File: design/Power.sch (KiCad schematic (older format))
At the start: 14 parts, among them U2 TC2117

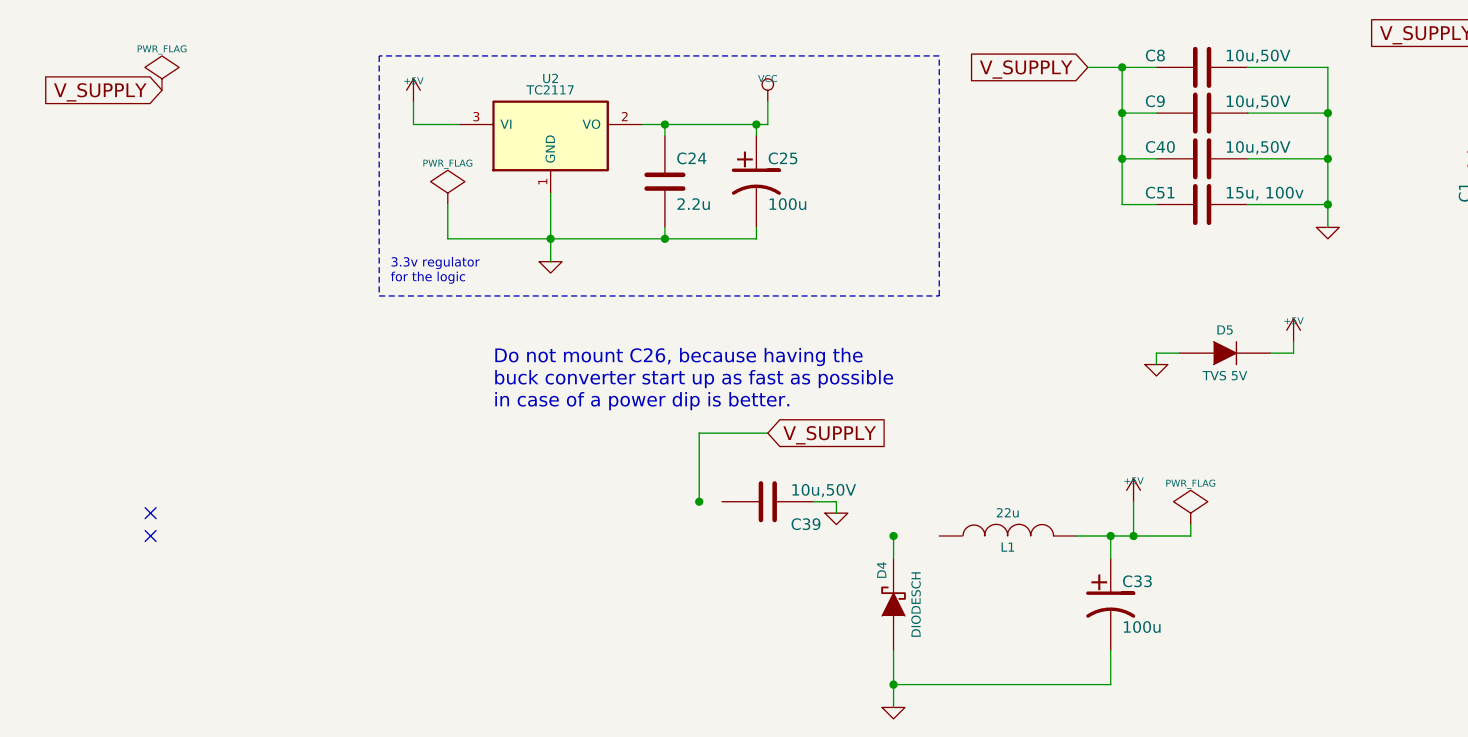
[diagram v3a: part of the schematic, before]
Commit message: Removed 5V power level. Integrated isolated CAN bus driver.
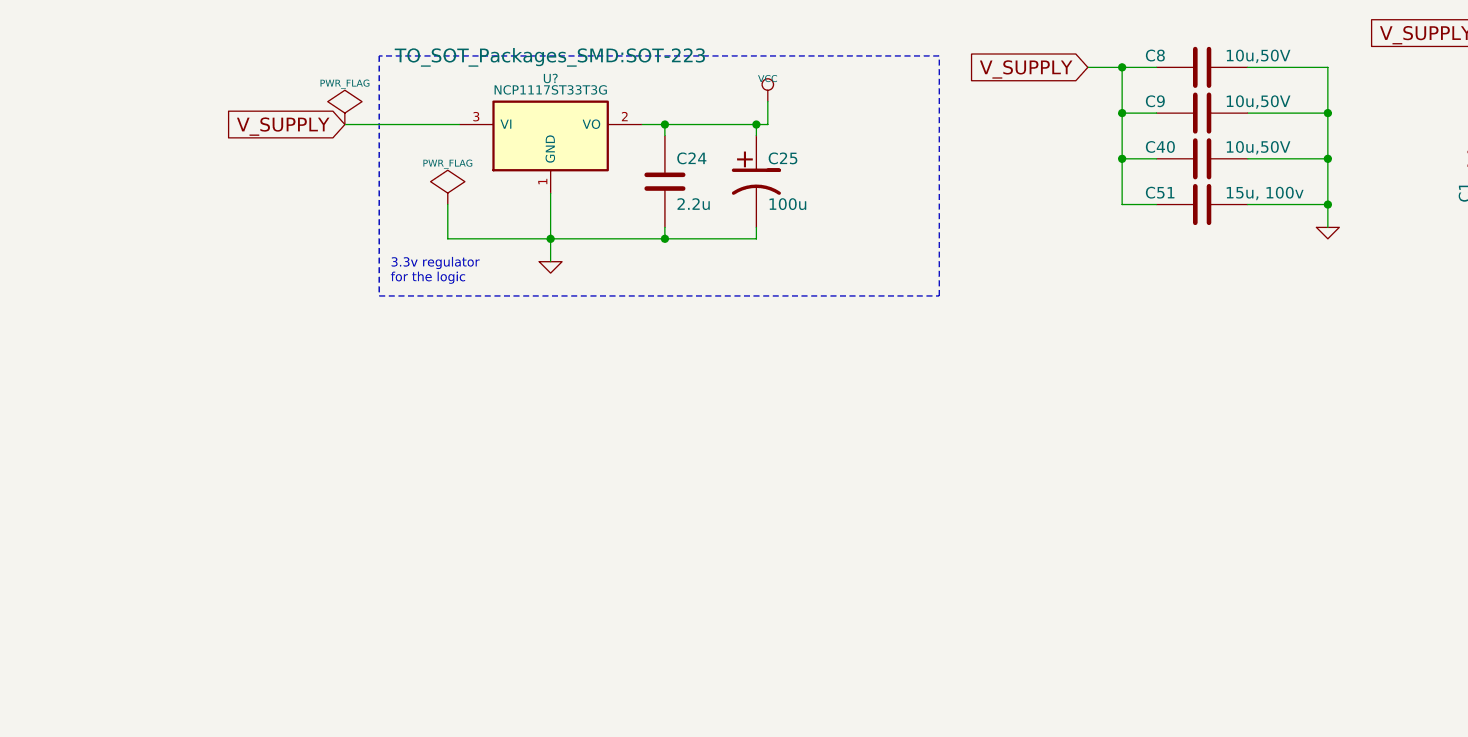
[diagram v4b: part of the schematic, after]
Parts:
- removed C33: 100u, w_smd_cap:c_tant_B, symbol CP1-RESCUE-BLDC_4
- removed C39: 10u,50V, SMD_Packages:SMD-1206, symbol C-RESCUE-BLDC_4
- removed D4: DIODESCH, Diodes_SMD:Diode-SMA_Handsoldering, symbol DIODESCH
- removed D5: TVS 5V, w_smd_diode:do214ac, symbol DIODE
- removed L1: 22u, w_smd_inductors:inductor_smd_8x5mm, symbol INDUCTOR
- removed U2: TC2117, SMD_Packages:SOT-223, symbol NCP1117ST33T3G
- added U?: NCP1117ST33T3G, TO_SOT_Packages_SMD:SOT-223, symbol NCP1117ST33T3G
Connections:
- net GND: now also U?.1 (GND)
- net VCC: now also U?.2 (VO)
- net V_SUPPLY: now also U?.3 (VI)
- no-connect marks 2 -> 0
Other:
- note removed: "Do not mount C26, because having the\nbuck converter start up as fast as possible\nin case of a power dip is better."
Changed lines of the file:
@@
 $Descr A4 11693 8268
 encoding utf-8
-Sheet 6 10
+Sheet 9 10
 Title "BLDC Driver 4.5"
 Date "25 Aug 2014"
@@
 $EndDescr
 $Comp
-L DIODESCH D4
-U 1 1 504F8F01
-P 7800 3250
-F 0 "D4" H 7950 3300 40  0000 C CNN
-F 1 "DIODESCH" H 7800 3150 40  0000 C CNN
-F 2 "Diodes_SMD:Diode-SMA_Handsoldering" H 7800 3250 60  0001 C CNN
-F 3 "" H 7800 3250 60  0001 C CNN
-	1    7800 3250
-	0    -1   -1   0
-$EndComp
-$Comp
-L INDUCTOR L1
-U 1 1 504FBBC5
-P 8300 2950
-F 0 "L1" V 8250 2950 40  0000 C CNN
-F 1 "22u" V 8400 2950 40  0000 C CNN
-F 2 "w_smd_inductors:inductor_smd_8x5mm" H 8300 2950 60  0001 C CNN
-F 3 "" H 8300 2950 60  0001 C CNN
-	1    8300 2950
-	0    -1   -1   0
-$EndComp
-$Comp
-L CP1-RESCUE-BLDC_4 C33
-U 1 1 504FBC81
-P 8750 3250
-F 0 "C33" H 8800 3350 50  0000 L CNN
-F 1 "100u" H 8800 3150 50  0000 L CNN
-F 2 "w_smd_cap:c_tant_B" H 8750 3250 60  0001 C CNN
-F 3 "" H 8750 3250 60  0001 C CNN
-	1    8750 3250
-	1    0    0    -1
-$EndComp
-$Comp
-L GND-RESCUE-BLDC_4 #PWR053
-U 1 1 504FBEC1
-P 7800 3700
-F 0 "#PWR053" H 7800 3700 30  0001 C CNN
-F 1 "GND" H 7800 3630 30  0001 C CNN
-F 2 "" H 7800 3700 60  0001 C CNN
-F 3 "" H 7800 3700 60  0001 C CNN
-	1    7800 3700
-	1    0    0    -1
-$EndComp
-$Comp
-L +5V #PWR054
-U 1 1 504FBFA1
-P 8850 2800
-F 0 "#PWR054" H 8850 2890 20  0001 C CNN
-F 1 "+5V" H 8850 2890 30  0000 C CNN
-F 2 "" H 8850 2800 60  0001 C CNN
-F 3 "" H 8850 2800 60  0001 C CNN
-	1    8850 2800
-	1    0    0    -1
-$EndComp
-$Comp
 L C-RESCUE-BLDC_4 C24
 U 1 1 50500B3A
@@
 $EndComp
 $Comp
-L +5V #PWR062
-U 1 1 50500BBC
-P 5700 1050
-F 0 "#PWR062" H 5700 1140 20  0001 C CNN
-F 1 "+5V" H 5700 1140 30  0000 C CNN
-F 2 "" H 5700 1050 60  0001 C CNN
-F 3 "" H 5700 1050 60  0001 C CNN
-	1    5700 1050
-	1    0    0    -1
-$EndComp
-$Comp
-L PWR_FLAG #FLG064
-U 1 1 50510100
-P 9100 2900
-F 0 "#FLG064" H 9100 2995 30  0001 C CNN
-F 1 "PWR_FLAG" H 9100 3080 30  0000 C CNN
-F 2 "" H 9100 2900 60  0001 C CNN
-F 3 "" H 9100 2900 60  0001 C CNN
-	1    9100 2900
-	1    0    0    -1
-$EndComp
-$Comp
 L PWR_FLAG #FLG065
 U 1 1 505104A0
@@
 L PWR_FLAG #FLG066
 U 1 1 505105A5
-P 4600 1000
-F 0 "#FLG066" H 4600 1095 30  0001 C CNN
-F 1 "PWR_FLAG" H 4600 1180 30  0000 C CNN
-F 2 "" H 4600 1000 60  0001 C CNN
-F 3 "" H 4600 1000 60  0001 C CNN
-	1    4600 1000
-	1    0    0    -1
-$EndComp
-$Comp
-L GND-RESCUE-BLDC_4 #PWR067
-U 1 1 5051337C
-P 7550 2850
-F 0 "#PWR067" H 7550 2850 30  0001 C CNN
-F 1 "GND" H 7550 2780 30  0001 C CNN
-F 2 "" H 7550 2850 60  0001 C CNN
-F 3 "" H 7550 2850 60  0001 C CNN
-	1    7550 2850
+P 5400 1150
+F 0 "#FLG066" H 5400 1245 30  0001 C CNN
+F 1 "PWR_FLAG" H 5400 1330 30  0000 C CNN
+F 2 "" H 5400 1150 60  0001 C CNN
+F 3 "" H 5400 1150 60  0001 C CNN
+	1    5400 1150
 	1    0    0    -1
 $EndComp
-NoConn ~ 4550 2850
-NoConn ~ 4550 2950
-$Comp
-L C-RESCUE-BLDC_4 C39
-U 1 1 505AC7E9
-P 7250 2800
-F 0 "C39" V 7350 2900 50  0000 L CNN
-F 1 "10u,50V" V 7200 2900 50  0000 L CNN
-F 2 "SMD_Packages:SMD-1206" H 7250 2800 60  0001 C CNN
-F 3 "" H 7250 2800 60  0001 C CNN
-	1    7250 2800
-	0    1    1    0
-$EndComp
-Text GLabel 7250 2500 2    60   Input ~ 0
-V_SUPPLY
 $Comp
 L C-RESCUE-BLDC_4 C51
@@
 	-1   0    0    1
 $EndComp
-$Comp
-L NCP1117ST33T3G U2
-U 1 1 53E7AF36
-P 6300 1200
-F 0 "U2" H 6300 1450 40  0000 C CNN
-F 1 "TC2117" H 6300 1400 40  0000 C CNN
-F 2 "SMD_Packages:SOT-223" H 6300 1200 60  0001 C CNN
-F 3 "" H 6300 1200 60  0000 C CNN
-	1    6300 1200
-	1    0    0    -1
-$EndComp
 Text GLabel 10400 750  0    60   Input ~ 0
 V_SUPPLY
-Text GLabel 4600 1000 0    60   Input ~ 0
+Text GLabel 5400 1150 0    60   Input ~ 0
 V_SUPPLY
 Text GLabel 8650 900  0    60   Input ~ 0
@@
 $EndBitmap
 Wire Wire Line
-	7800 3450 7800 3700
-Wire Wire Line
-	7800 3600 8750 3600
-Wire Wire Line
-	8750 3600 8750 3450
-Wire Wire Line
-	8600 2950 9100 2950
-Wire Wire Line
-	8750 2950 8750 3050
-Wire Wire Line
-	7800 3050 7800 2950
-Connection ~ 7800 2950
-Connection ~ 7800 3600
-Wire Wire Line
-	8850 2950 8850 2800
-Connection ~ 8750 2950
-Wire Wire Line
 	5850 1650 7200 1650
 Wire Wire Line
@@
 	6700 1150 7250 1150
 Wire Wire Line
-	5900 1150 5700 1150
-Wire Wire Line
-	5700 1150 5700 1050
-Wire Wire Line
-	9100 2950 9100 2900
-Connection ~ 8850 2950
-Wire Wire Line
 	5850 1650 5850 1500
 Wire Wire Line
-	6950 2500 6950 2800
-Wire Wire Line
-	7450 2800 7550 2800
-Wire Wire Line
-	7550 2800 7550 2850
-Connection ~ 6950 2800
-Wire Wire Line
-	6950 2500 7250 2500
-Wire Wire Line
 	9700 1500 9350 1500
 Wire Wire Line
@@
 AB D8 39 0B 59 91 9E DF A8 2A 5B EE 54 3A FD 71 ED 71 2F 29 C3 82 EC 80 87 06 6E C3 98 10 30 3B
 62 9A BB 2D 03 B8 C4 64 FC B5 26 AC 13 9B D1 39 40 41 C1 D6 78 4C 84 BF 94 F0 6F E1 BF 96 F0 0F
-FF 77 E2 FF 1F 0F 43 55 32 21 1C 08 16 00 00 00 00 49 45 4E 44 AE 42 60 82 25
+FF 77 E2 FF 1F 0F 43 55 32 21 1C 08 16 00 00 00 00 49 45 4E 44 AE 42 60 82 53
 EndData
 $EndBitmap
 $Comp
-L DIODE D5
-U 1 1 548EDCBC
-P 9250 2150
-F 0 "D5" H 9250 2250 40  0000 C CNN
-F 1 "TVS 5V" H 9250 2050 40  0000 C CNN
-F 2 "w_smd_diode:do214ac" H 9250 2150 60  0001 C CNN
-F 3 "" H 9250 2150 60  0000 C CNN
-	1    9250 2150
-	1    0    0    -1
-$EndComp
-$Comp
-L +5V #PWR070
-U 1 1 548EDECA
-P 9550 2100
-F 0 "#PWR070" H 9550 2190 20  0001 C CNN
-F 1 "+5V" H 9550 2190 30  0000 C CNN
-F 2 "" H 9550 2100 60  0001 C CNN
-F 3 "" H 9550 2100 60  0001 C CNN
-	1    9550 2100
-	1    0    0    -1
-$EndComp
-$Comp
-L GND-RESCUE-BLDC_4 #PWR071
-U 1 1 548EDF07
-P 8950 2200
-F 0 "#PWR071" H 8950 2200 30  0001 C CNN
-F 1 "GND" H 8950 2130 30  0001 C CNN
-F 2 "" H 8950 2200 60  0001 C CNN
-F 3 "" H 8950 2200 60  0001 C CNN
-	1    8950 2200
-	1    0    0    -1
-$EndComp
-Wire Wire Line
-	8950 2200 8950 2150
-Wire Wire Line
-	8950 2150 9050 2150
-Wire Wire Line
-	9450 2150 9550 2150
-Wire Wire Line
-	9550 2150 9550 2100
-$Comp
 L GND-RESCUE-BLDC_4 #PWR072
 U 1 1 548F3DC0
@@
 	1    0    0    -1
 $EndComp
-Text Notes 6050 2400 0    60   ~ 0
-Do not mount C26, because having the\nbuck converter start up as fast as possible\nin case of a power dip is better.
+$Comp
+L NCP1117ST33T3G U?
+U 1 1 55DF064F
+P 6300 1200
+F 0 "U?" H 6300 1450 40  0000 C CNN
+F 1 "NCP1117ST33T3G" H 6300 1400 40  0000 C CNN
+F 2 "TO_SOT_Packages_SMD:SOT-223" H 6300 1550 60  0000 C CNN
+F 3 "" H 6300 1200 60  0000 C CNN
+	1    6300 1200
+	1    0    0    -1
+$EndComp
+Wire Wire Line
+	5900 1150 5400 1150
 $EndSCHEMATC

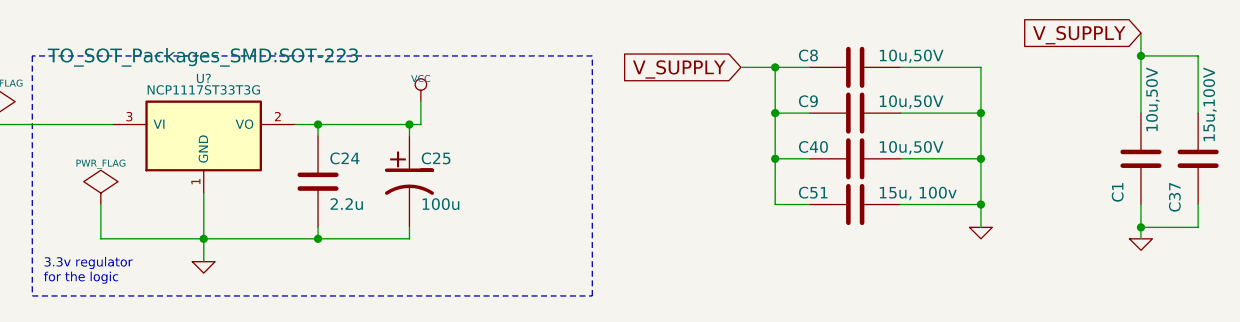
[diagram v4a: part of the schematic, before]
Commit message: First complete draft of the schematics.
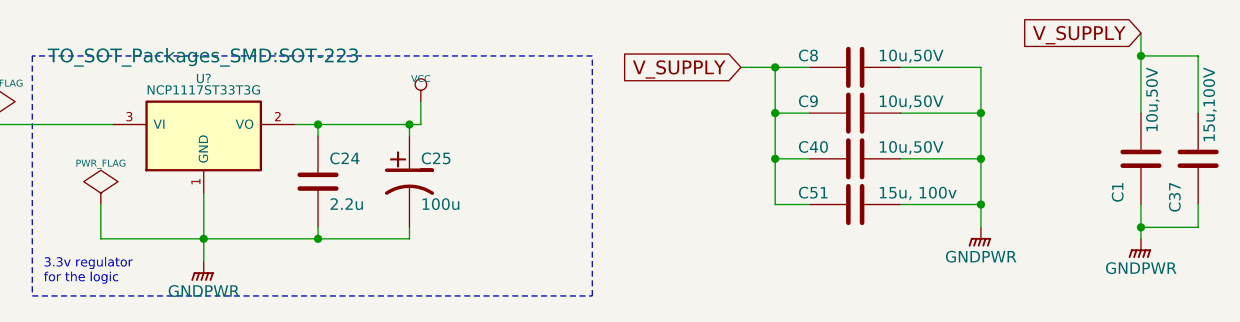
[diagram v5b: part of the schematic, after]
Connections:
- net GND renamed GNDPWR
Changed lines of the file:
@@
 $Descr A4 11693 8268
 encoding utf-8
-Sheet 9 10
+Sheet 9 11
 Title "BLDC Driver 4.5"
 Date "25 Aug 2014"
@@
 $EndComp
 $Comp
-L GND-RESCUE-BLDC_4 #PWR060
-U 1 1 50500B40
-P 6300 1750
-F 0 "#PWR060" H 6300 1750 30  0001 C CNN
-F 1 "GND" H 6300 1680 30  0001 C CNN
-F 2 "" H 6300 1750 60  0001 C CNN
-F 3 "" H 6300 1750 60  0001 C CNN
-	1    6300 1750
-	1    0    0    -1
-$EndComp
-$Comp
 L VCC #PWR061
 U 1 1 50500B46
@@
 $EndComp
 $Comp
-L GND-RESCUE-BLDC_4 #PWR069
-U 1 1 510944D0
-P 9700 1600
-F 0 "#PWR069" H 9700 1600 30  0001 C CNN
-F 1 "GND" H 9700 1530 30  0001 C CNN
-F 2 "" H 9700 1600 60  0001 C CNN
-F 3 "" H 9700 1600 60  0001 C CNN
-	1    9700 1600
-	1    0    0    -1
-$EndComp
-$Comp
 L C-RESCUE-BLDC_4 C1
 U 1 1 523435A0
@@
 00 FD 87 A8 17 00 00 00 00 F4 1F A2 5E 00 00 00 00 D0 7F 88 7A 01 00 00 00 40 FF 21 EA 05 00 00
 00 00 FD 87 A8 17 00 00 00 00 F4 1F A2 5E 00 00 00 00 D0 7F 88 7A 01 00 00 00 40 FF 21 EA 05 00
-00 00 00 FD F7 3F 90 37 91 24 49 74 FD E2 00 00 00 00 49 45 4E 44 AE 42 60 82 00
+00 00 00 FD F7 3F 90 37 91 24 49 74 FD E2 00 00 00 00 49 45 4E 44 AE 42 60 82 01
 EndData
 $EndBitmap
@@
 AB D8 39 0B 59 91 9E DF A8 2A 5B EE 54 3A FD 71 ED 71 2F 29 C3 82 EC 80 87 06 6E C3 98 10 30 3B
 62 9A BB 2D 03 B8 C4 64 FC B5 26 AC 13 9B D1 39 40 41 C1 D6 78 4C 84 BF 94 F0 6F E1 BF 96 F0 0F
-FF 77 E2 FF 1F 0F 43 55 32 21 1C 08 16 00 00 00 00 49 45 4E 44 AE 42 60 82 53
+FF 77 E2 FF 1F 0F 43 55 32 21 1C 08 16 00 00 00 00 49 45 4E 44 AE 42 60 82 50
 EndData
 $EndBitmap
 $Comp
-L GND-RESCUE-BLDC_4 #PWR072
-U 1 1 548F3DC0
-P 10400 1650
-F 0 "#PWR072" H 10400 1650 30  0001 C CNN
-F 1 "GND" H 10400 1580 30  0001 C CNN
-F 2 "" H 10400 1650 60  0001 C CNN
-F 3 "" H 10400 1650 60  0001 C CNN
-	1    10400 1650
-	1    0    0    -1
-$EndComp
-$Comp
 L NCP1117ST33T3G U?
 U 1 1 55DF064F
@@
 Wire Wire Line
 	5900 1150 5400 1150
+$Comp
+L GNDPWR #PWR?
+U 1 1 55E7501A
+P 6300 1750
+F 0 "#PWR?" H 6300 1550 50  0001 C CNN
+F 1 "GNDPWR" H 6300 1620 50  0000 C CNN
+F 2 "" H 6300 1700 60  0000 C CNN
+F 3 "" H 6300 1700 60  0000 C CNN
+	1    6300 1750
+	1    0    0    -1
+$EndComp
+$Comp
+L GNDPWR #PWR?
+U 1 1 55E75054
+P 9700 1600
+F 0 "#PWR?" H 9700 1400 50  0001 C CNN
+F 1 "GNDPWR" H 9700 1470 50  0000 C CNN
+F 2 "" H 9700 1550 60  0000 C CNN
+F 3 "" H 9700 1550 60  0000 C CNN
+	1    9700 1600
+	1    0    0    -1
+$EndComp
+$Comp
+L GNDPWR #PWR?
+U 1 1 55E7507A
+P 10400 1650
+F 0 "#PWR?" H 10400 1450 50  0001 C CNN
+F 1 "GNDPWR" H 10400 1520 50  0000 C CNN
+F 2 "" H 10400 1600 60  0000 C CNN
+F 3 "" H 10400 1600 60  0000 C CNN
+	1    10400 1650
+	1    0    0    -1
+$EndComp
 $EndSCHEMATC

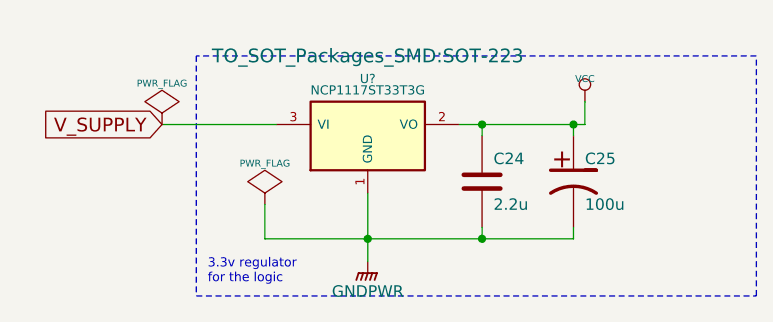
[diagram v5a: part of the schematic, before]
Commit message: Assigned some footprints.
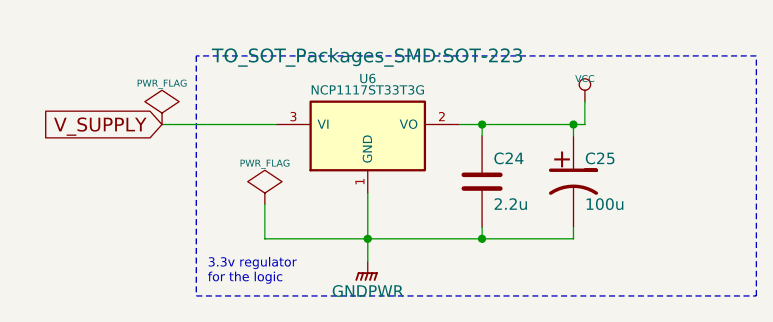
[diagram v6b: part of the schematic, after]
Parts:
- C1, C40, C8, C9: footprint SMD_Packages:SMD-1206 -> Capacitors_SMD:C_1206
- C24: footprint SMD_Packages:SMD-0603_c -> Capacitors_SMD:C_0603
- C25: footprint w_smd_cap:c_tant_B -> Capacitors_Tantalum_SMD:TantalC_SizeB_EIA-3528_HandSoldering
- C37, C51: footprint w_smd_cap:c_2220 -> Capacitors_SMD:C_2220
- gave numbers to parts that had none: 1
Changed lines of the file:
@@
 F 0 "C24" H 6850 1500 50  0000 L CNN
 F 1 "2.2u" H 6850 1300 50  0000 L CNN
-F 2 "SMD_Packages:SMD-0603_c" H 6800 1400 60  0001 C CNN
+F 2 "Capacitors_SMD:C_0603" H 6800 1400 60  0001 C CNN
 F 3 "" H 6800 1400 60  0001 C CNN
 	1    6800 1400
@@
 $EndComp
 $Comp
-L VCC #PWR061
+L VCC #PWR040
 U 1 1 50500B46
 P 7250 1050
-F 0 "#PWR061" H 7250 1150 30  0001 C CNN
+F 0 "#PWR040" H 7250 1150 30  0001 C CNN
 F 1 "VCC" H 7250 1150 30  0000 C CNN
 F 2 "" H 7250 1050 60  0001 C CNN
@@
 F 0 "C25" H 7250 1500 50  0000 L CNN
 F 1 "100u" H 7250 1300 50  0000 L CNN
-F 2 "w_smd_cap:c_tant_B" H 7200 1400 60  0001 C CNN
+F 2 "Capacitors_Tantalum_SMD:TantalC_SizeB_EIA-3528_HandSoldering" H 7200 1400 60  0001 C CNN
 F 3 "" H 7200 1400 60  0001 C CNN
 	1    7200 1400
@@
 $EndComp
 $Comp
-L PWR_FLAG #FLG065
+L PWR_FLAG #FLG041
 U 1 1 505104A0
 P 5850 1500
-F 0 "#FLG065" H 5850 1595 30  0001 C CNN
+F 0 "#FLG041" H 5850 1595 30  0001 C CNN
 F 1 "PWR_FLAG" H 5850 1680 30  0000 C CNN
 F 2 "" H 5850 1500 60  0001 C CNN
@@
 $EndComp
 $Comp
-L PWR_FLAG #FLG066
+L PWR_FLAG #FLG042
 U 1 1 505105A5
 P 5400 1150
-F 0 "#FLG066" H 5400 1245 30  0001 C CNN
+F 0 "#FLG042" H 5400 1245 30  0001 C CNN
 F 1 "PWR_FLAG" H 5400 1330 30  0000 C CNN
 F 2 "" H 5400 1150 60  0001 C CNN
@@
 F 0 "C51" V 9100 1250 50  0000 L CNN
 F 1 "15u, 100v" V 9100 1600 50  0000 L CNN
-F 2 "w_smd_cap:c_2220" H 9150 1500 60  0001 C CNN
+F 2 "Capacitors_SMD:C_2220" H 9150 1500 60  0001 C CNN
 F 3 "" H 9150 1500 60  0001 C CNN
 	1    9150 1500
@@
 F 0 "C1" V 10500 1400 50  0000 L CNN
 F 1 "10u,50V" V 10350 900 50  0000 L CNN
-F 2 "SMD_Packages:SMD-1206" H 10400 1300 60  0001 C CNN
+F 2 "Capacitors_SMD:C_1206" H 10400 1300 60  0001 C CNN
 F 3 "" H 10400 1300 60  0001 C CNN
 	1    10400 1300
@@
 F 0 "C37" V 10750 1400 50  0000 L CNN
 F 1 "15u,100V" V 10600 900 50  0000 L CNN
-F 2 "w_smd_cap:c_2220" H 10650 1300 60  0001 C CNN
+F 2 "Capacitors_SMD:C_2220" H 10650 1300 60  0001 C CNN
 F 3 "" H 10650 1300 60  0001 C CNN
 	1    10650 1300
@@
 F 0 "C40" V 9100 1050 50  0000 L CNN
 F 1 "10u,50V" V 9100 1400 50  0000 L CNN
-F 2 "SMD_Packages:SMD-1206" H 9150 1300 60  0001 C CNN
+F 2 "Capacitors_SMD:C_1206" H 9150 1300 60  0001 C CNN
 F 3 "" H 9150 1300 60  0001 C CNN
 	1    9150 1300
@@
 F 0 "C9" V 9100 850 50  0000 L CNN
 F 1 "10u,50V" V 9100 1200 50  0000 L CNN
-F 2 "SMD_Packages:SMD-1206" H 9150 1100 60  0001 C CNN
+F 2 "Capacitors_SMD:C_1206" H 9150 1100 60  0001 C CNN
 F 3 "" H 9150 1100 60  0001 C CNN
 	1    9150 1100
@@
 F 0 "C8" V 9100 650 50  0000 L CNN
 F 1 "10u,50V" V 9100 1000 50  0000 L CNN
-F 2 "SMD_Packages:SMD-1206" H 9150 900 60  0001 C CNN
+F 2 "Capacitors_SMD:C_1206" H 9150 900 60  0001 C CNN
 F 3 "" H 9150 900 60  0001 C CNN
 	1    9150 900
@@
 00 FD 87 A8 17 00 00 00 00 F4 1F A2 5E 00 00 00 00 D0 7F 88 7A 01 00 00 00 40 FF 21 EA 05 00 00
 00 00 FD 87 A8 17 00 00 00 00 F4 1F A2 5E 00 00 00 00 D0 7F 88 7A 01 00 00 00 40 FF 21 EA 05 00
-00 00 00 FD F7 3F 90 37 91 24 49 74 FD E2 00 00 00 00 49 45 4E 44 AE 42 60 82 01
+00 00 00 FD F7 3F 90 37 91 24 49 74 FD E2 00 00 00 00 49 45 4E 44 AE 42 60 82 04
 EndData
 $EndBitmap
@@
 AB D8 39 0B 59 91 9E DF A8 2A 5B EE 54 3A FD 71 ED 71 2F 29 C3 82 EC 80 87 06 6E C3 98 10 30 3B
 62 9A BB 2D 03 B8 C4 64 FC B5 26 AC 13 9B D1 39 40 41 C1 D6 78 4C 84 BF 94 F0 6F E1 BF 96 F0 0F
-FF 77 E2 FF 1F 0F 43 55 32 21 1C 08 16 00 00 00 00 49 45 4E 44 AE 42 60 82 50
+FF 77 E2 FF 1F 0F 43 55 32 21 1C 08 16 00 00 00 00 49 45 4E 44 AE 42 60 82 16
 EndData
 $EndBitmap
 $Comp
-L NCP1117ST33T3G U?
+L NCP1117ST33T3G U6
 U 1 1 55DF064F
 P 6300 1200
-F 0 "U?" H 6300 1450 40  0000 C CNN
+F 0 "U6" H 6300 1450 40  0000 C CNN
 F 1 "NCP1117ST33T3G" H 6300 1400 40  0000 C CNN
 F 2 "TO_SOT_Packages_SMD:SOT-223" H 6300 1550 60  0000 C CNN
@@
 	5900 1150 5400 1150
 $Comp
-L GNDPWR #PWR?
+L GNDPWR #PWR043
 U 1 1 55E7501A
 P 6300 1750
-F 0 "#PWR?" H 6300 1550 50  0001 C CNN
+F 0 "#PWR043" H 6300 1550 50  0001 C CNN
 F 1 "GNDPWR" H 6300 1620 50  0000 C CNN
 F 2 "" H 6300 1700 60  0000 C CNN
@@
 $EndComp
 $Comp
-L GNDPWR #PWR?
+L GNDPWR #PWR044
 U 1 1 55E75054
 P 9700 1600
-F 0 "#PWR?" H 9700 1400 50  0001 C CNN
+F 0 "#PWR044" H 9700 1400 50  0001 C CNN
 F 1 "GNDPWR" H 9700 1470 50  0000 C CNN
 F 2 "" H 9700 1550 60  0000 C CNN
@@
 $EndComp
 $Comp
-L GNDPWR #PWR?
+L GNDPWR #PWR045
 U 1 1 55E7507A
 P 10400 1650
-F 0 "#PWR?" H 10400 1450 50  0001 C CNN
+F 0 "#PWR045" H 10400 1450 50  0001 C CNN
 F 1 "GNDPWR" H 10400 1520 50  0000 C CNN
 F 2 "" H 10400 1600 60  0000 C CNN
